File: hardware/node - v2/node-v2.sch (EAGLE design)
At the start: 54 parts, among them IC1 HYPERTRIANGLE_TCS3472FN, Q1 32.768kHz, Q2 24MHz, U1 INA322_DGK_8, U2 LMV551_DBV_5, X1 BU-SMA-1-7HOLE

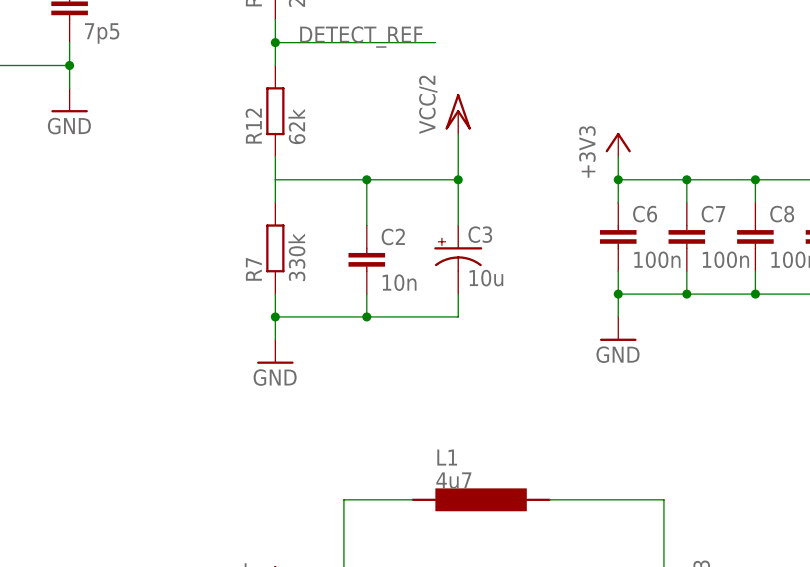
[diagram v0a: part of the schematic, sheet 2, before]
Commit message: NODEHW: Further updates to capacitor values found as part of #6
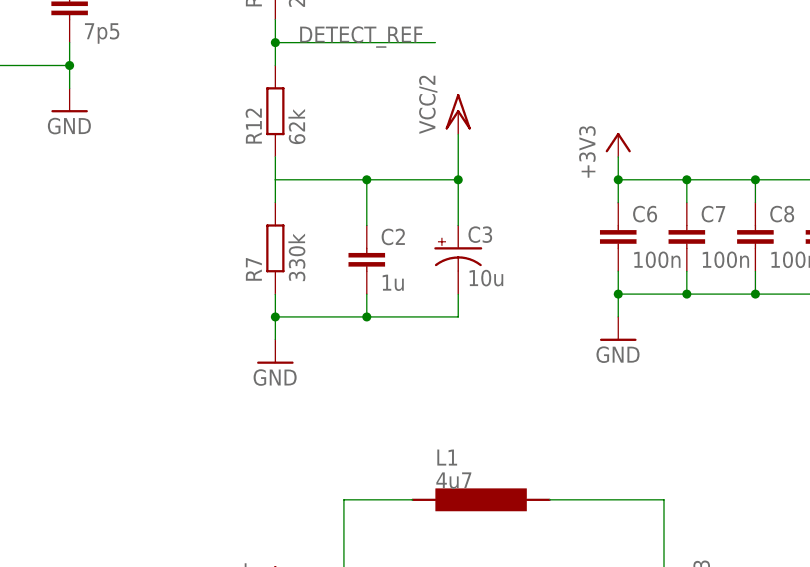
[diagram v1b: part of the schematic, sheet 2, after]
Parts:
- C2: value 10n -> 1u
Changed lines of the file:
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@@
 <part name="GND3" library="supply1" deviceset="GND" device=""/>
 <part name="R7" library="resistor" deviceset="R-EU_" device="0204/7" value="330k"/>
-<part name="C2" library="SparkFun-Capacitors" deviceset="CAP" device="PTH" value="10n"/>
+<part name="C2" library="SparkFun-Capacitors" deviceset="CAP" device="PTH" value="1u"/>
 <part name="C3" library="SparkFun-Capacitors" deviceset="CAP_POL" device="PTH2" value="10u"/>
 <part name="P+4" library="supply1" deviceset="VCC/2" device=""/>

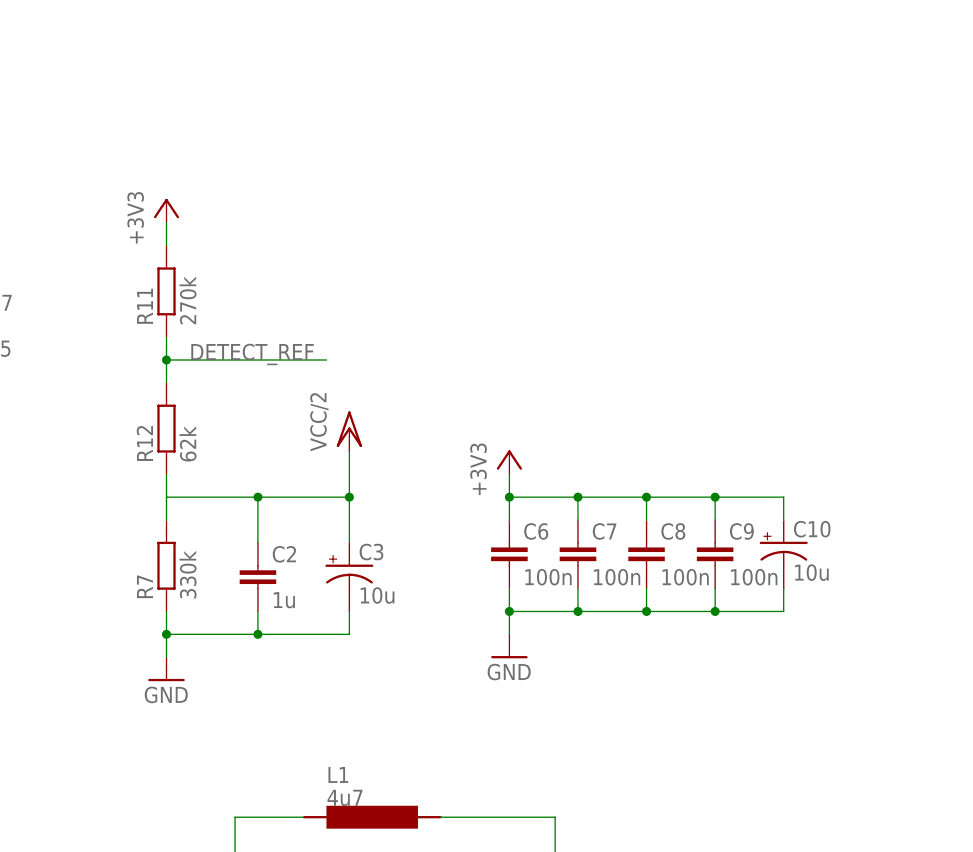
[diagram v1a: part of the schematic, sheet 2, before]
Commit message: NODEHW: Completed v2 rework. There are no ADC pins available for #9 therefore it is wontfix.
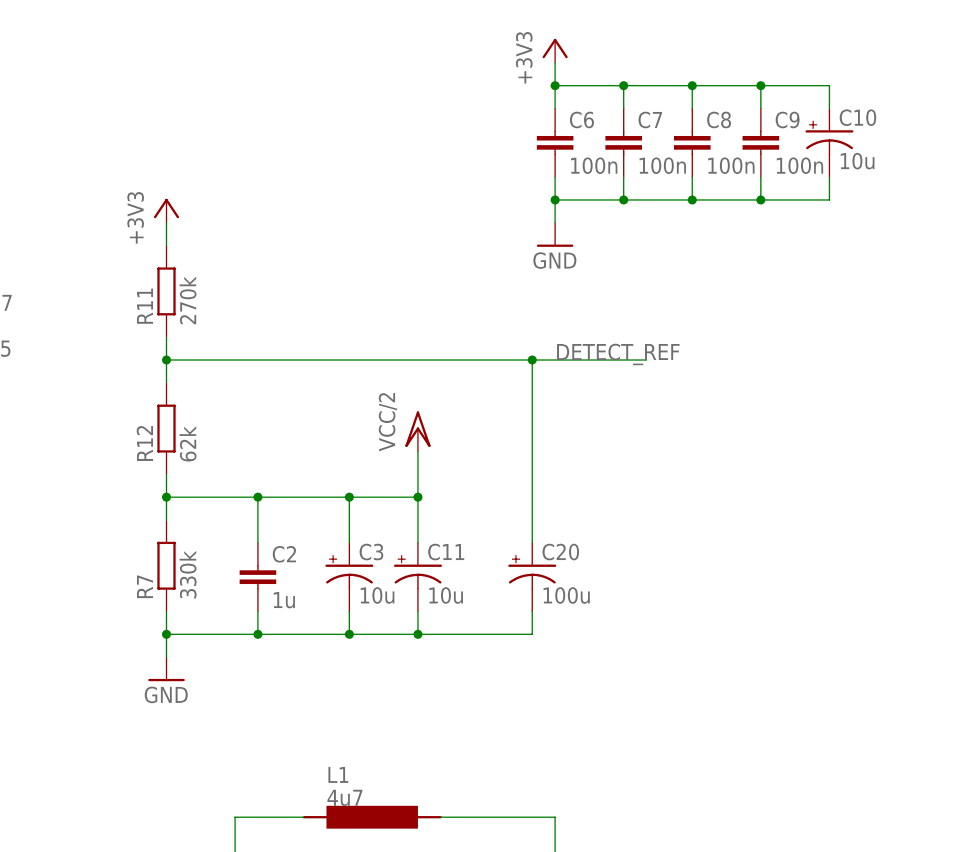
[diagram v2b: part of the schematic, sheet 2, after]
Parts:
- added C11: 10u, SparkFun-Capacitors:CAP_POLPTH2
- added C20: 100u, SparkFun-Capacitors:CAP_POLPTH2
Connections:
- removed net RADIO_MISO: RADIO.MISO, U$2G$3.PC1
- new net N$1: RADIO.MISO, U$2G$3.PD6
- net DETECT_REF: now also C20.+
- net GND: now also C11.-, C20.-
- net RADIO_MOSI: now also U$2G$3.PD7; no longer U$2G$3.PC0
- net SW_ADDR_7: now also U$2G$3.PC0; no longer U$2G$3.PD7
- net SW_ADDR_8: now also U$2G$3.PC1; no longer U$2G$3.PD6
- net VCC/2: now also C11.+
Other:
- moved on the sheet: C10, C6, C7, C8, C9
